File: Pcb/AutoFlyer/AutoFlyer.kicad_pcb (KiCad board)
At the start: 2 copper layers, 35.6 x 17.8 mm, 19 parts, among them J1 Screw_Terminal_1x02, J2 Programmer, J3 Battery, SW1 SW_Push, U1 ATTINY45-20PU, U2 LD1117S33TR_SOT223, U3 H-Bridge-DMHC3025LSD, X1 HOLE, X2 HOLE

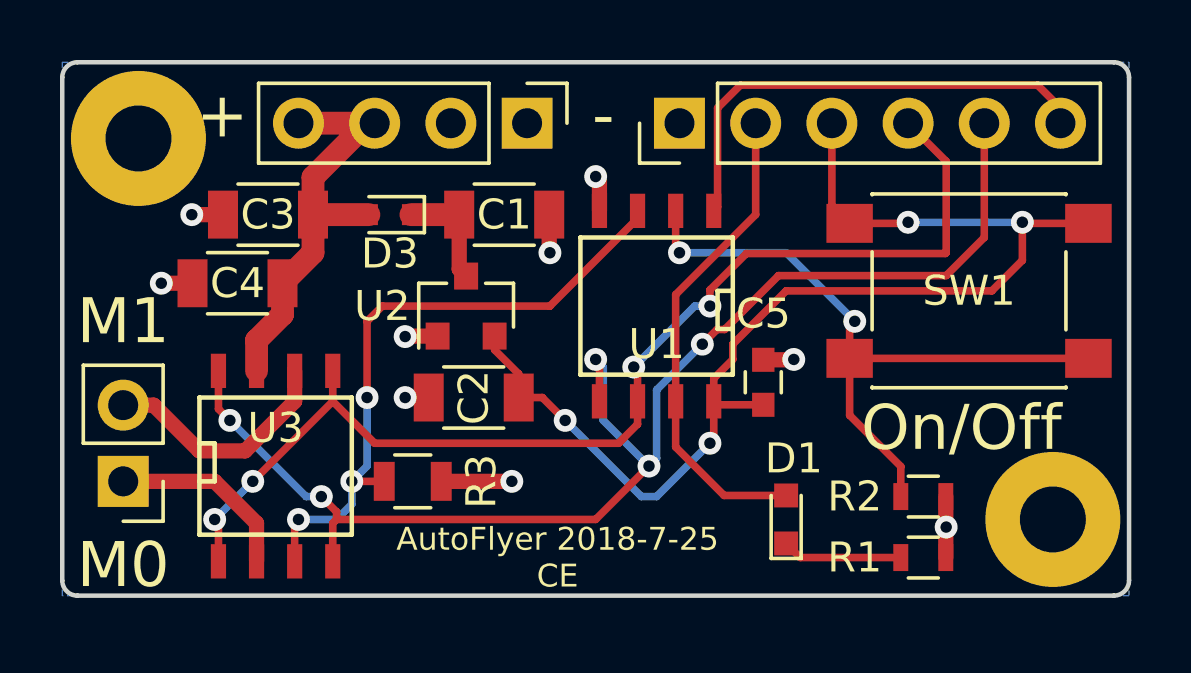
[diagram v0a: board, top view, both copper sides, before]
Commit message: Add autoflyer pcb
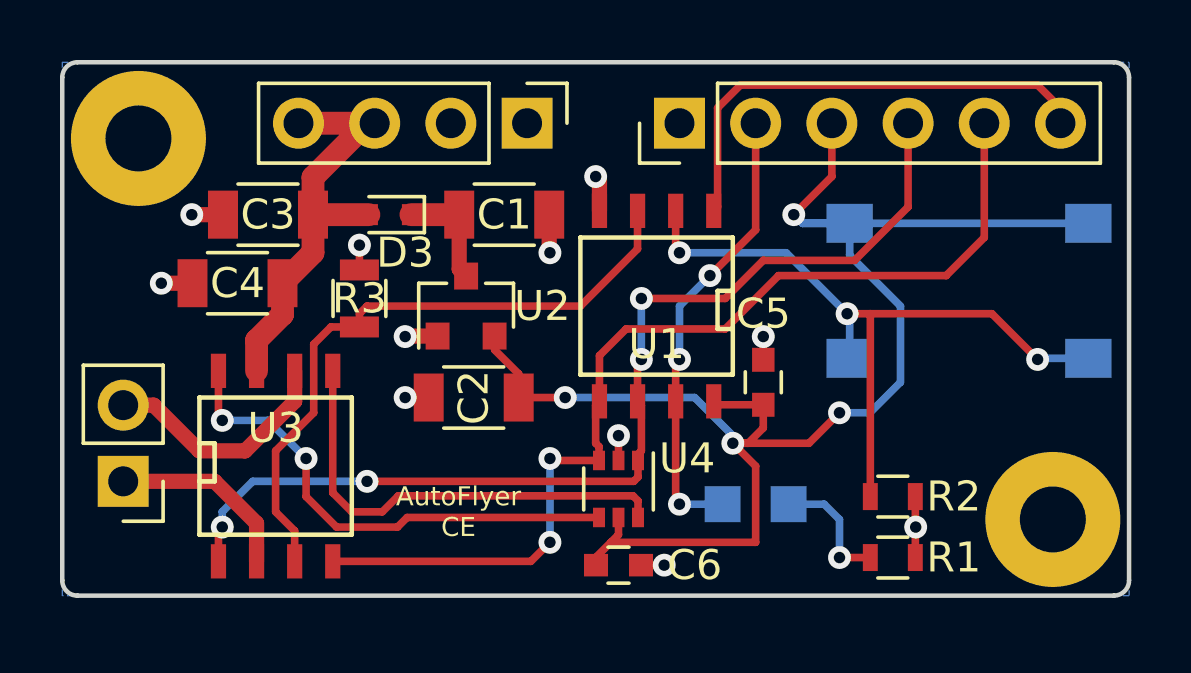
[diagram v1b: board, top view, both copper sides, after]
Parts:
- added C6: 0.1uF, Capacitors_SMD:C_0603, F.Cu at (43.9, 42.2)
- added U4: Inverter2, TO_SOT_Packages_SMD:SOT-363_SC-70-6, F.Cu at (43.9, 39.6)
- D1: footprint LEDs:LED_0603 -> LEDs:LED_0805; moved to B.Cu
- SW1: moved to B.Cu
- moved R3 6.35 mm to (35.3, 33.3), turned to 90 degrees
- moved D1 1.14 mm to (48.5, 40.1), turned to 180 degrees
- moved R1 1.02 mm to (53.1, 41.9)
- moved R2 1.02 mm to (53.1, 39.9)
- turned SW1 to 0 degrees
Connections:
- U3 pad 5: /miso -> Net-(U3-Pad5)
- U3 pad 8: /mosi -> Net-(U3-Pad8)
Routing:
- net Net-(U3-Pad8): track 0.00 -> 16.6 mm, vias 0 -> 2
- net Net-(U3-Pad5): track 0.00 -> 15.3 mm
- net +3V3: track 40.0 -> 52.8 mm
- net /mosi: track 44.7 -> 33.8 mm, vias 5 -> 2
- net /miso: track 38.1 -> 35.4 mm
- net Net-(R2-Pad2): track 22.8 -> 24.2 mm, vias 2 -> 3
- net /sck: track 16.3 -> 15.3 mm, vias 0 -> 3
- net /Shunt: track 21.5 -> 21.9 mm, vias 3 -> 0
- net Net-(D1-Pad1): track 4.02 -> 4.20 mm, vias 0 -> 1
- net GND: track 11.8 -> 11.9 mm, vias 9 -> 11
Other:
- board text added: "AutoFlyer 18.8.2 CE"
- board text added: "AutoFlyer CE"
- board text removed: "AutoFlyer 2018-7-25 CE"

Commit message: Update auto flyer and some documentation
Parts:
- removed C4: 10uF, Capacitors_SMD:C_1206
- removed C6: 0.1uF, Capacitors_SMD:C_0603
- removed U4: Inverter2, TO_SOT_Packages_SMD:SOT-363_SC-70-6
- U1: value ATTINY45-20PU -> ATTINY44-20SSU; footprint SMD_Packages:SOIC-8-N -> Housings_SOIC:SOIC-14_3.9x8.7mm_Pitch1.27mm
- moved J2 12.7 mm to (58.7, 27.4), turned to 270 degrees
- moved R3 8.92 mm to (38.4, 41.7), turned to 0 degrees
- moved C5 5.68 mm to (46.2, 31.0), turned to 0 degrees
- moved U1 3.14 mm to (46.0, 36.6), turned to 0 degrees
- moved D1 2.38 mm to (50.8, 40.8), turned to 90 degrees
- moved C3 2.32 mm to (30.5, 32.0)
- moved C2 2.09 mm to (38.6, 38.6)
- moved U2 1.60 mm to (38.4, 35.1)
- moved D3 1.43 mm to (35.1, 31.2)
- moved C1 1.28 mm to (39.3, 31.5)
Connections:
- D1 pad 2: /sck -> /led
- J3 pad 2: GND -> Net-(J3-Pad2)
- J3 pad 3: +6V -> Net-(J3-Pad2)
- R3 pad 1: /Shunt -> /shunt
- U1 pad 1: /rst -> +3V3
- U1 pad 2: Net-(R2-Pad2) -> /c3
- U1 pad 3: /Shunt -> /c2
- U1 pad 4: GND -> /rst
- U1 pad 5: /mosi -> /c1
- U1 pad 6: /miso -> /c0
- U1 pad 7: /sck -> /mosi
- U1 pad 8: +3V3 -> /miso
- U3 pad 1: /miso -> /c0
- U3 pad 3: /Shunt -> /shunt
- U3 pad 4: /mosi -> /c1
- U3 pad 5: Net-(U3-Pad5) -> /c2
- U3 pad 8: Net-(U3-Pad8) -> /c3
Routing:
- net /shunt: track 0.00 -> 23.9 mm
- net /Shunt: track 21.9 -> 0.00 mm
- net /miso: track 35.4 -> 16.8 mm, vias 4 -> 1
- net /mosi: track 33.8 -> 15.4 mm, vias 2 -> 1
- net Net-(U3-Pad8): track 16.6 -> 0.00 mm, vias 2 -> 0
- net /c0: track 0.00 -> 16.1 mm, vias 0 -> 2
- net Net-(U3-Pad5): track 15.3 -> 0.00 mm
- net /c3: track 0.00 -> 14.5 mm, vias 0 -> 4
- net /c1: track 0.00 -> 10.9 mm, vias 0 -> 2
- net +3V3: track 52.8 -> 43.5 mm, vias 4 -> 0
- net /c2: track 0.00 -> 9.01 mm, vias 0 -> 2
- net Net-(R2-Pad2): track 24.2 -> 16.0 mm, vias 3 -> 2
- net GND: track 11.9 -> 17.5 mm, vias 11 -> 8
- net /led: track 0.00 -> 4.28 mm, vias 0 -> 1
- net /rst: track 16.1 -> 12.4 mm
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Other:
- board text added: "AutoFlyer 18.10.12 CE"
- board text added: "B0+"
- board text added: "B0-"
- board text added: "B1+"
- board text added: "B1-"
- board text removed: "+"
- board text removed: "-"
- board text removed: "AutoFlyer 18.8.2 CE"
